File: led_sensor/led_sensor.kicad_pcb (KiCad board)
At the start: 4 copper layers, 54 parts

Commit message: switched symbols
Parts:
- removed LED0: XZCFBB53W-8VF, SamacSys_Parts:HSMA-C380
- added U1: XZCFBB53W-8VF-xzcfbb53w-8vf, SamacSys_Parts:HSMA-C380, F.Cu at (39.7, 126.9)

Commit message: final Rev1 changes. increased heatsink area, flipped LEDs again, increased button mount hole size
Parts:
- moved LED7 8.46 mm to (269.8, 135.3), turned to 180 degrees
- moved LED3 8.45 mm to (137.1, 135.4), turned to 180 degrees
- moved LED5 8.42 mm to (203.4, 135.3), turned to 180 degrees
- moved LED2 8.41 mm to (104.2, 135.2), turned to 180 degrees
- moved LED0 8.39 mm to (38.5, 135.2), turned to 180 degrees
- moved LED4 8.36 mm to (170.5, 135.2), turned to 180 degrees
- moved LED6 8.35 mm to (236.6, 135.2), turned to 180 degrees
- moved LED1 8.21 mm to (72.1, 135.2), turned to 180 degrees
- renumbered U1 to LED0
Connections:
- LED0 pad 1: /CCin -> /dpin
- LED0 pad 2: /dpin -> /CCin
- LED1 pad 1: /CCin -> /gin
- LED1 pad 2: /gin -> /CCin
- LED2 pad 1: /CCin -> /fin
- LED2 pad 2: /fin -> /CCin
- LED3 pad 1: /CCin -> /ein
- LED3 pad 2: /ein -> /CCin
- LED4 pad 1: /CCin -> /din
- LED4 pad 2: /din -> /CCin
- LED5 pad 1: /CCin -> /cin
- LED5 pad 2: /cin -> /CCin
- LED6 pad 1: /CCin -> /bin
- LED6 pad 2: /bin -> /CCin
- LED7 pad 1: /CCin -> /ain
- LED7 pad 2: /ain -> /CCin
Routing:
- net /CCin: track 276.2 -> 268.7 mm
- net /ain: track 57.5 -> 58.1 mm

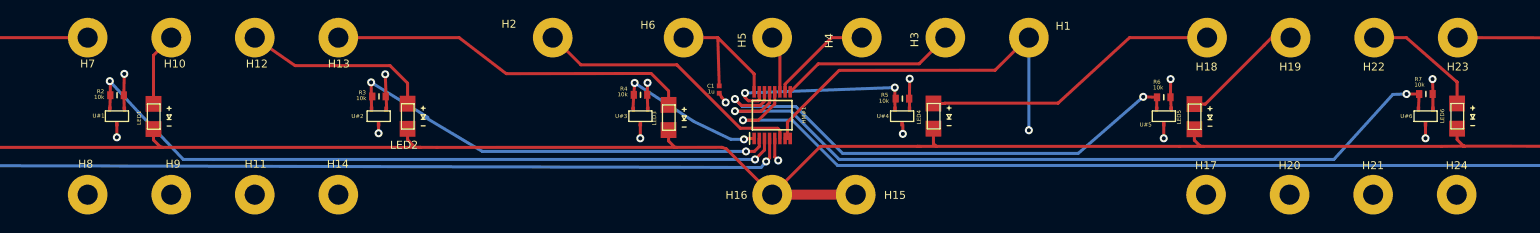
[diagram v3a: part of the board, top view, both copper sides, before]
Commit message: edited main board headers for buttons, daughterboard power
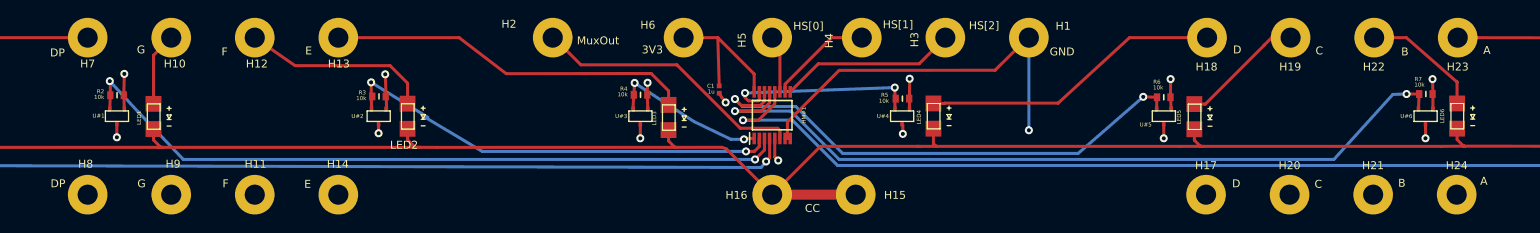
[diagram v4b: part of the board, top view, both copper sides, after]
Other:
- board text added: "3V3"
- board text added: "A"
- board text added: "B"
- board text added: "C"
- board text added: "CC"
- board text added: "D"
- board text added: "DP"
- board text added: "E"
- board text added: "F"
- board text added: "G"
- board text added: "GND"
- board text added: "HS[0]"
- board text added: "HS[1]"
- board text added: "HS[2]"
- board text added: "MuxOut"
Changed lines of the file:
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@@
   (general
     (thickness 1.6)
-    (drawings 61)
+    (drawings 84)
     (tracks 309)
     (zones 0)
@@
       (net 16 /dpin))
   )
+  (gr_text HS[2] (at 177.3555 119.634) (layer F.SilkS)
+    (effects (font (size 1 1) (thickness 0.15)))
+  )
+  (gr_text HS[1] (at 166.497 119.507) (layer F.SilkS)
+    (effects (font (size 1 1) (thickness 0.15)))
+  )
+  (gr_text HS[0] (at 155.194 119.6975) (layer F.SilkS)
+    (effects (font (size 1 1) (thickness 0.15)))
+  )
+  (gr_text GND (at 187.198 122.936) (layer F.SilkS)
+    (effects (font (size 1 1) (thickness 0.15)))
+  )
+  (gr_text 3V3 (at 135.509 122.682) (layer F.SilkS)
+    (effects (font (size 1 1) (thickness 0.15)))
+  )
+  (gr_text CC (at 155.702 142.6845) (layer F.SilkS)
+    (effects (font (size 1 1) (thickness 0.15)))
+  )
+  (gr_text A (at 240.792 122.7455) (layer F.SilkS)
+    (effects (font (size 1 1) (thickness 0.15)))
+  )
+  (gr_text A (at 240.411 139.2555) (layer F.SilkS)
+    (effects (font (size 1 1) (thickness 0.15)))
+  )
+  (gr_text B (at 230.0605 139.5095) (layer F.SilkS)
+    (effects (font (size 1 1) (thickness 0.15)))
+  )
+  (gr_text B (at 230.4415 122.936) (layer F.SilkS)
+    (effects (font (size 1 1) (thickness 0.15)))
+  )
+  (gr_text C (at 219.6465 122.809) (layer F.SilkS)
+    (effects (font (size 1 1) (thickness 0.15)))
+  )
+  (gr_text C (at 219.5195 139.6365) (layer F.SilkS)
+    (effects (font (size 1 1) (thickness 0.15)))
+  )
+  (gr_text D (at 209.169 139.573) (layer F.SilkS)
+    (effects (font (size 1 1) (thickness 0.15)))
+  )
+  (gr_text D (at 209.296 122.682) (layer F.SilkS)
+    (effects (font (size 1 1) (thickness 0.15)))
+  )
+  (gr_text MuxOut (at 128.651 121.539) (layer F.SilkS)
+    (effects (font (size 1 1) (thickness 0.15)))
+  )
+  (gr_text E (at 92.1385 122.809) (layer F.SilkS)
+    (effects (font (size 1 1) (thickness 0.15)))
+  )
+  (gr_text E (at 92.0115 139.6365) (layer F.SilkS)
+    (effects (font (size 1 1) (thickness 0.15)))
+  )
+  (gr_text F (at 81.661 139.573) (layer F.SilkS)
+    (effects (font (size 1 1) (thickness 0.15)))
+  )
+  (gr_text F (at 81.534 122.936) (layer F.SilkS)
+    (effects (font (size 1 1) (thickness 0.15)))
+  )
+  (gr_text G (at 70.993 122.682) (layer F.SilkS)
+    (effects (font (size 1 1) (thickness 0.15)))
+  )
+  (gr_text G (at 71.0565 139.573) (layer F.SilkS)
+    (effects (font (size 1 1) (thickness 0.15)))
+  )
+  (gr_text DP (at 60.5155 139.573) (layer F.SilkS)
+    (effects (font (size 1 1) (thickness 0.15)))
+  )
+  (gr_text DP (at 60.452 123.063) (layer F.SilkS)
+    (effects (font (size 1 1) (thickness 0.15)))
+  )
   (gr_text "Aedan Frazier\nBilal Salha\nMax Baer\nThomas Munsell" (at 24.13 121.9835) (layer F.SilkS)

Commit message: gerbers
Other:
- board outline added: 264.2 x 25.4 mm
- rule pad_to_mask_clearance: 0.051 -> 0
